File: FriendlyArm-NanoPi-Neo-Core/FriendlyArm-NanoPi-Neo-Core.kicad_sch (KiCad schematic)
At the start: 11 parts, among them J1 Conn_02x12_Odd_Even, J2 Conn_02x12_Odd_Even, J3 Conn_02x10_Odd_Even, J4 USB_OTG, J5 Micro_SD_Card

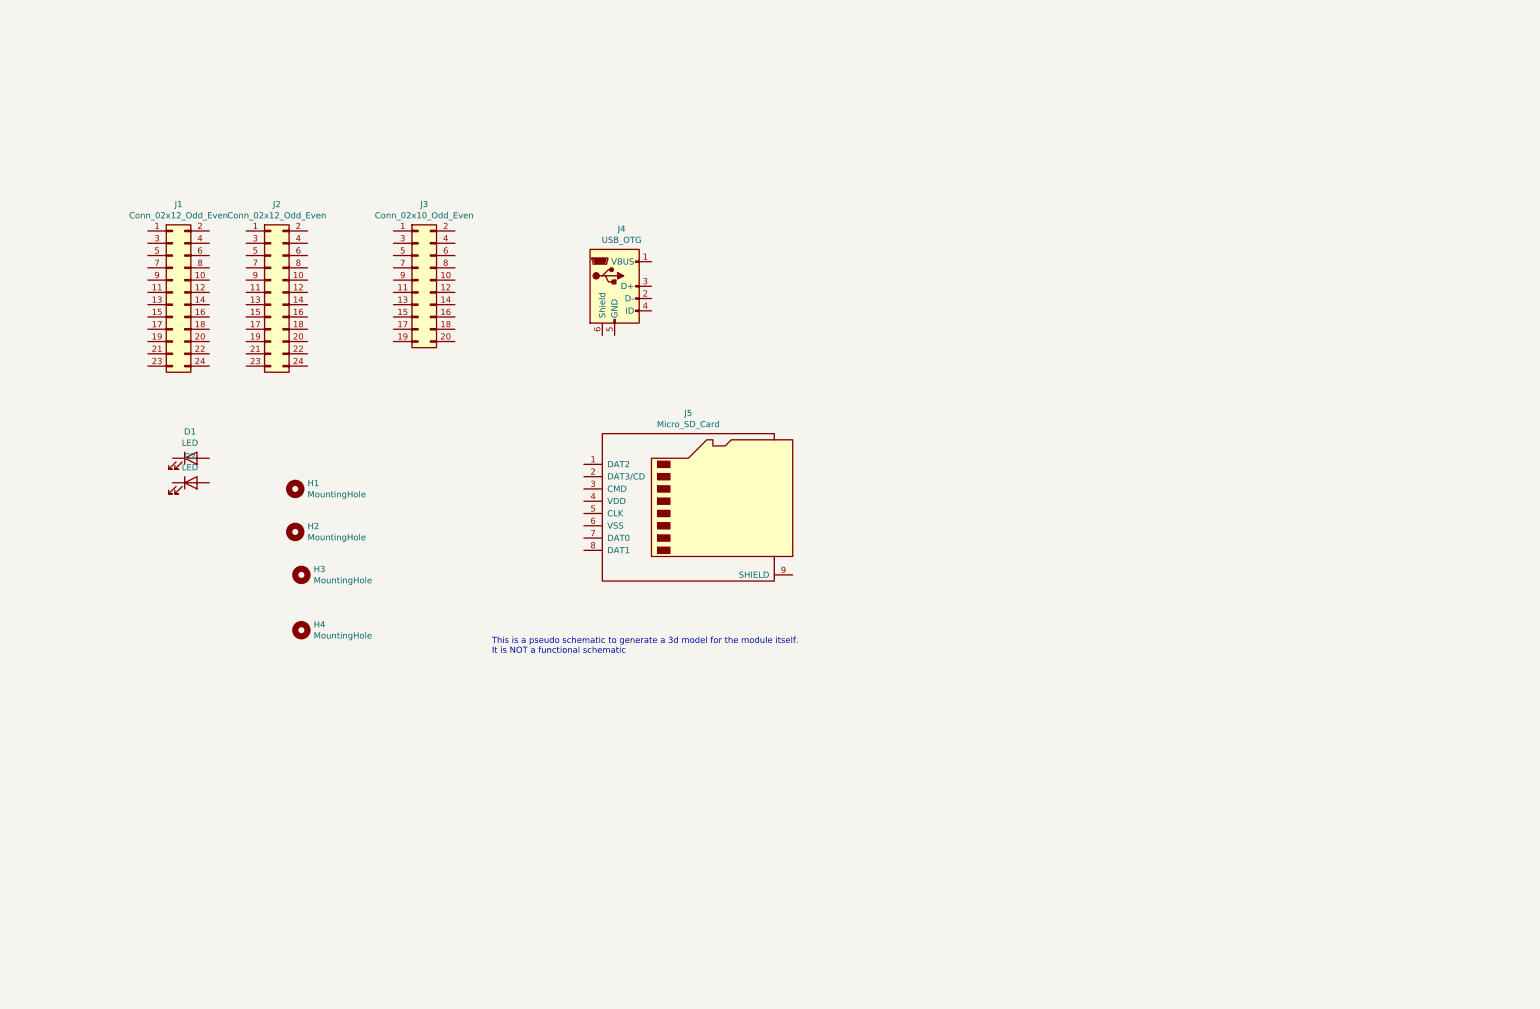
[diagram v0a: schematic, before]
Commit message: nanopi-core: completely overhaul model
Properly numerically align, place all big bgas, label headers
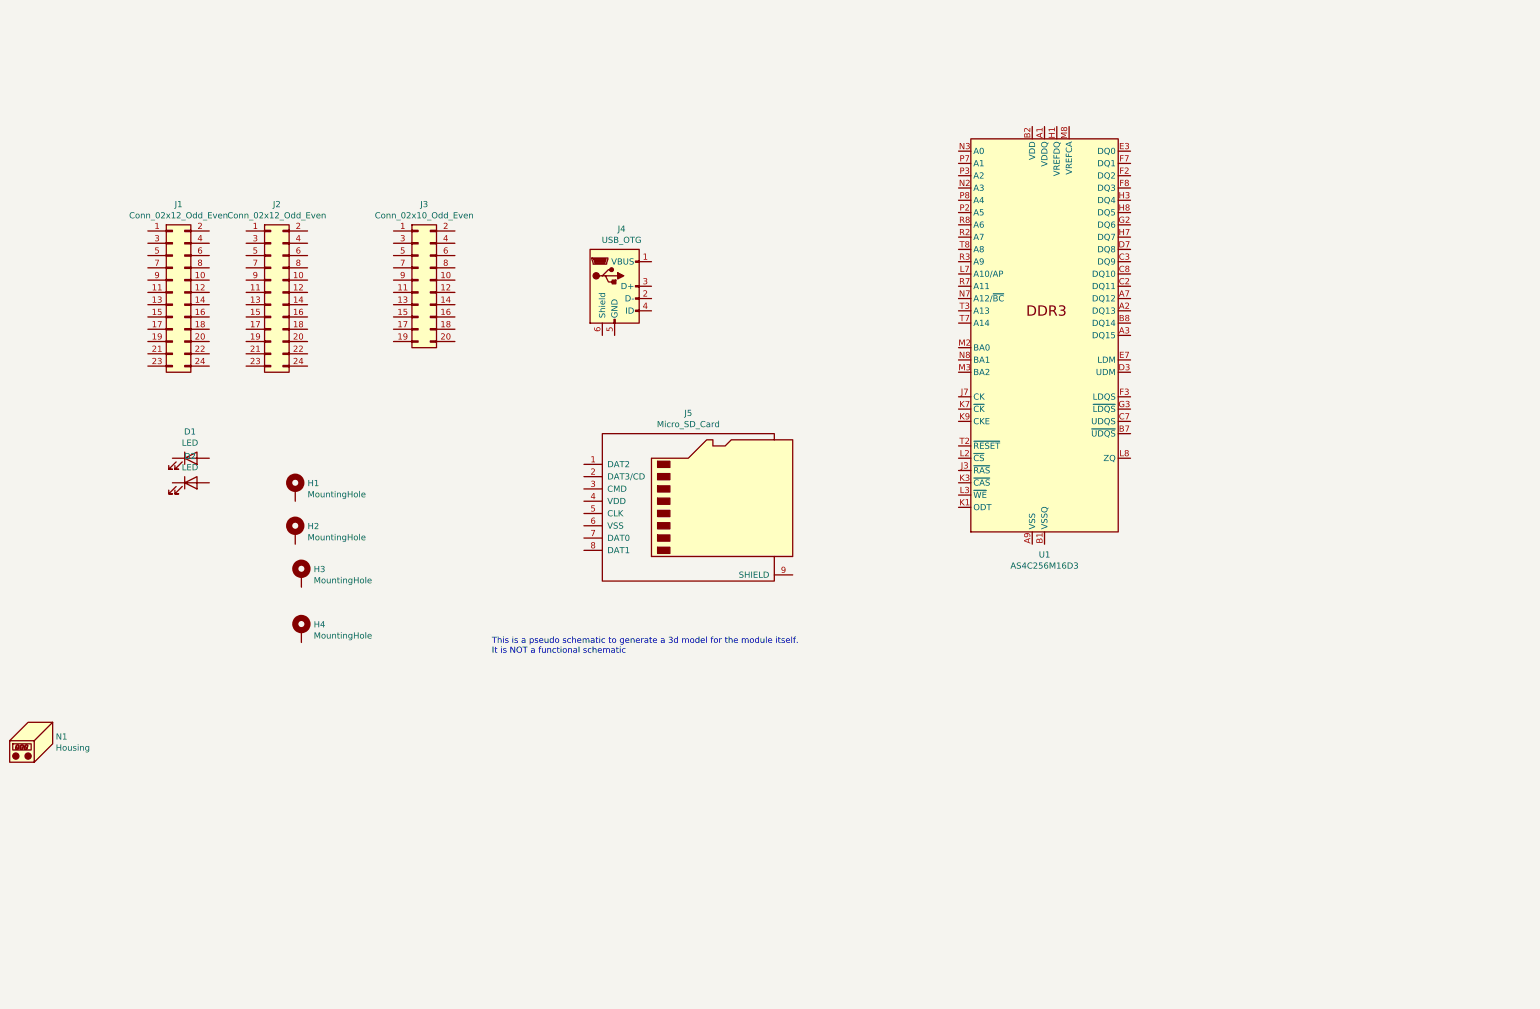
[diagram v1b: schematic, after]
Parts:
- added N1: Housing, Package_BGA:BGA-256_14.0x14.0mm_Layout16x16_P0.8mm_Ball0.45mm_Pad0.32mm_NSMD, symbol Mechanical:Housing
- added U1: AS4C256M16D3, Package_BGA:BGA-96_9.0x13.0mm_Layout2x3x16_P0.8mm, symbol Memory_RAM:AS4C256M16D3
- D1, D2: footprint LED_SMD:LED_0603_1608Metric_Castellated -> LED_SMD:LED_0603_1608Metric
- H1, H2, H3, H4: footprint MountingHole:MountingHole_2.2mm_M2 -> MountingHole:MountingHole_3mm_Pad; symbol Mechanical:MountingHole -> Mechanical:MountingHole_Pad
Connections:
- new net: U1.A1 (VDDQ), U1.A8 (VDDQ), U1.C1 (VDDQ), U1.C9 (VDDQ), U1.D2 (VDDQ), U1.E9 (VDDQ), U1.F1 (VDDQ), U1.H2 (VDDQ), U1.H9 (VDDQ)
- new net: U1.A9 (VSS), U1.B3 (VSS), U1.E1 (VSS), U1.G8 (VSS), U1.J2 (VSS), U1.J8 (VSS), U1.M1 (VSS), U1.M9 (VSS), U1.P1 (VSS), U1.P9 (VSS), U1.T1 (VSS), U1.T9 (VSS)
- new net: U1.B1 (VSSQ), U1.B9 (VSSQ), U1.D1 (VSSQ), U1.D8 (VSSQ), U1.E2 (VSSQ), U1.E8 (VSSQ), U1.F9 (VSSQ), U1.G1 (VSSQ), U1.G9 (VSSQ)
- new net: U1.B2 (VDD), U1.D9 (VDD), U1.G7 (VDD), U1.K2 (VDD), U1.K8 (VDD), U1.N1 (VDD), U1.N9 (VDD), U1.R1 (VDD), U1.R9 (VDD)
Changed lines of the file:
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@@
     (effects (font (size 1.27 1.27)) (justify left bottom))
   )
-  (symbol (lib_id "Mechanical:MountingHole") (at 86.36 97.79 0) (unit 1)
+  (symbol (lib_id "Mechanical:MountingHole_Pad") (at 86.36 97.79 0) (unit 1)
     (in_bom yes) (on_board yes)
     (property "Reference" "H1" (id 0) (at 88.9 96.6216 0)
@@
       (effects (font (size 1.27 1.27)) (justify left))
     )
-    (property "Footprint" "MountingHole:MountingHole_2.2mm_M2" (id 2) (at 86.36 97.79 0)
+    (property "Footprint" "MountingHole:MountingHole_3mm_Pad" (id 2) (at 86.36 97.79 0)
       (effects (font (size 1.27 1.27)) hide)
     )
@@
       (effects (font (size 1.27 1.27)) hide)
     )
-  )
-  (symbol (lib_id "Mechanical:MountingHole") (at 86.36 106.68 0) (unit 1)
+    (pin "1")
+  )
+  (symbol (lib_id "Mechanical:MountingHole_Pad") (at 86.36 106.68 0) (unit 1)
     (in_bom yes) (on_board yes)
     (property "Reference" "H2" (id 0) (at 88.9 105.5116 0)
@@
       (effects (font (size 1.27 1.27)) (justify left))
     )
-    (property "Footprint" "MountingHole:MountingHole_2.2mm_M2" (id 2) (at 86.36 106.68 0)
+    (property "Footprint" "MountingHole:MountingHole_3mm_Pad" (id 2) (at 86.36 106.68 0)
       (effects (font (size 1.27 1.27)) hide)
     )
@@
       (effects (font (size 1.27 1.27)) hide)
     )
-  )
-  (symbol (lib_id "Mechanical:MountingHole") (at 87.63 115.57 0) (unit 1)
+    (pin "1")
+  )
+  (symbol (lib_id "Mechanical:MountingHole_Pad") (at 87.63 115.57 0) (unit 1)
     (in_bom yes) (on_board yes)
     (property "Reference" "H3" (id 0) (at 90.17 114.4016 0)
@@
       (effects (font (size 1.27 1.27)) (justify left))
     )
-    (property "Footprint" "MountingHole:MountingHole_2.2mm_M2" (id 2) (at 87.63 115.57 0)
+    (property "Footprint" "MountingHole:MountingHole_3mm_Pad" (id 2) (at 87.63 115.57 0)
       (effects (font (size 1.27 1.27)) hide)
     )
@@
       (effects (font (size 1.27 1.27)) hide)
     )
-  )
-  (symbol (lib_id "Mechanical:MountingHole") (at 87.63 127 0) (unit 1)
+    (pin "1")
+  )
+  (symbol (lib_id "Mechanical:MountingHole_Pad") (at 87.63 127 0) (unit 1)
     (in_bom yes) (on_board yes)
     (property "Reference" "H4" (id 0) (at 90.17 125.8316 0)
@@
       (effects (font (size 1.27 1.27)) (justify left))
     )
-    (property "Footprint" "MountingHole:MountingHole_2.2mm_M2" (id 2) (at 87.63 127 0)
+    (property "Footprint" "MountingHole:MountingHole_3mm_Pad" (id 2) (at 87.63 127 0)
       (effects (font (size 1.27 1.27)) hide)
     )
@@
       (effects (font (size 1.27 1.27)) hide)
     )
+    (pin "1")
   )
   (symbol (lib_id "Device:LED") (at 64.77 91.44 0) (unit 1)
@@
     (property "Reference" "D1" (id 0) (at 64.5922 85.9536 0))
     (property "Value" "LED" (id 1) (at 64.5922 88.265 0))
-    (property "Footprint" "LED_SMD:LED_0603_1608Metric_Castellated" (id 2) (at 64.77 91.44 0)
+    (property "Footprint" "LED_SMD:LED_0603_1608Metric" (id 2) (at 64.77 91.44 0)
       (effects (font (size 1.27 1.27)) hide)
     )
@@
     (property "Reference" "D2" (id 0) (at 64.5922 91.0336 0))
     (property "Value" "LED" (id 1) (at 64.5922 93.345 0))
-    (property "Footprint" "LED_SMD:LED_0603_1608Metric_Castellated" (id 2) (at 64.77 96.52 0)
+    (property "Footprint" "LED_SMD:LED_0603_1608Metric" (id 2) (at 64.77 96.52 0)
       (effects (font (size 1.27 1.27)) hide)
     )
@@
     (pin "1")
     (pin "2")
+  )
+  (symbol (lib_id "Mechanical:Housing") (at 33.02 149.86 0) (unit 1)
+    (in_bom yes) (on_board yes)
+    (property "Reference" "N1" (id 0) (at 36.8301 149.0281 0)
+      (effects (font (size 1.27 1.27)) (justify left))
+    )
+    (property "Value" "Housing" (id 1) (at 36.8301 151.3268 0)
+      (effects (font (size 1.27 1.27)) (justify left))
+    )
+    (property "Footprint" "Package_BGA:BGA-256_14.0x14.0mm_Layout16x16_P0.8mm_Ball0.45mm_Pad0.32mm_NSMD" (id 2) (at 34.29 148.59 0)
+      (effects (font (size 1.27 1.27)) hide)
+    )
+    (property "Datasheet" "~" (id 3) (at 34.29 148.59 0)
+      (effects (font (size 1.27 1.27)) hide)
+    )
   )
   (symbol (lib_id "Connector:USB_OTG") (at 152.4 55.88 0) (unit 1)
@@
     (pin "9")
   )
+  (symbol (lib_id "Memory_RAM:AS4C256M16D3") (at 241.3 66.04 0) (unit 1)
+    (in_bom yes) (on_board yes)
+    (property "Reference" "U1" (id 0) (at 241.3 111.3854 0))
+    (property "Value" "AS4C256M16D3" (id 1) (at 241.3 113.6841 0))
+    (property "Footprint" "Package_BGA:BGA-96_9.0x13.0mm_Layout2x3x16_P0.8mm" (id 2) (at 240.03 20.32 0)
+      (effects (font (size 1.27 1.27)) hide)
+    )
+    (property "Datasheet" "https://www.alliancememory.com/wp-content/uploads/pdf/ddr3/4GB-AS4C256M16D3.pdf" (id 3) (at 240.03 -2.54 0)
+      (effects (font (size 1.27 1.27)) hide)
+    )
+    (pin "A1")
+    (pin "A8")
+    (pin "A9")
+    (pin "B1")
+    (pin "B2")
+    (pin "B3")
+    (pin "B9")
+    (pin "C1")
+    (pin "C9")
+    (pin "D1")
+    (pin "D2")
+    (pin "D8")
+    (pin "D9")
+    (pin "E1")
+    (pin "E2")
+    (pin "E3")
+    (pin "E8")
+    (pin "E9")
+    (pin "F1")
+    (pin "F2")
+    (pin "F7")
+    (pin "F8")
+    (pin "F9")
+    (pin "G1")
+    (pin "G2")
+    (pin "G7")
+    (pin "G8")
+    (pin "G9")
+    (pin "H1")
+    (pin "H2")
+    (pin "H3")
+    (pin "H7")
+    (pin "H8")
+    (pin "H9")
+    (pin "J2")
+    (pin "J8")
+    (pin "K2")
+    (pin "K8")
+    (pin "L2")
+    (pin "L7")
+    (pin "M1")
+    (pin "M9")
+    (pin "N1")
+    (pin "N2")
+    (pin "N3")
+    (pin "N7")
+    (pin "N9")
+    (pin "P1")
+    (pin "P2")
+    (pin "P3")
+    (pin "P7")
+    (pin "P8")
+    (pin "P9")
+    (pin "R1")
+    (pin "R2")
+    (pin "R3")
+    (pin "R7")
+    (pin "R8")
+    (pin "R9")
+    (pin "T1")
+    (pin "T2")
+    (pin "T3")
+    (pin "T7")
+    (pin "T8")
+    (pin "T9")
+    (pin "A2")
+    (pin "A3")
+    (pin "A7")
+    (pin "B7")
+    (pin "B8")
+    (pin "C2")
+    (pin "C3")
+    (pin "C7")
+    (pin "C8")
+    (pin "D3")
+    (pin "D7")
+    (pin "E7")
+    (pin "F3")
+    (pin "G3")
+    (pin "J1")
+    (pin "J3")
+    (pin "J7")
+    (pin "J9")
+    (pin "K1")
+    (pin "K3")
+    (pin "K7")
+    (pin "K9")
+    (pin "L1")
+    (pin "L3")
+    (pin "L8")
+    (pin "L9")
+    (pin "M2")
+    (pin "M3")
+    (pin "M7")
+    (pin "M8")
+    (pin "N8")
+  )
   (sheet_instances
     (path "/" (page "1"))
@@
   (symbol_instances
     (path "/00000000-0000-0000-0000-00005bf1d529"
-      (reference "D1") (unit 1) (value "LED") (footprint "LED_SMD:LED_0603_1608Metric_Castellated")
+      (reference "D1") (unit 1) (value "LED") (footprint "LED_SMD:LED_0603_1608Metric")
     )
     (path "/00000000-0000-0000-0000-00005bf1d9d2"
-      (reference "D2") (unit 1) (value "LED") (footprint "LED_SMD:LED_0603_1608Metric_Castellated")
+      (reference "D2") (unit 1) (value "LED") (footprint "LED_SMD:LED_0603_1608Metric")
     )
     (path "/00000000-0000-0000-0000-00005befb352"
-      (reference "H1") (unit 1) (value "MountingHole") (footprint "MountingHole:MountingHole_2.2mm_M2")
+      (reference "H1") (unit 1) (value "MountingHole") (footprint "MountingHole:MountingHole_3mm_Pad")
     )
     (path "/00000000-0000-0000-0000-00005befb57d"
-      (reference "H2") (unit 1) (value "MountingHole") (footprint "MountingHole:MountingHole_2.2mm_M2")
+      (reference "H2") (unit 1) (value "MountingHole") (footprint "MountingHole:MountingHole_3mm_Pad")
     )
     (path "/00000000-0000-0000-0000-00005befb66a"
-      (reference "H3") (unit 1) (value "MountingHole") (footprint "MountingHole:MountingHole_2.2mm_M2")
+      (reference "H3") (unit 1) (value "MountingHole") (footprint "MountingHole:MountingHole_3mm_Pad")
     )
     (path "/00000000-0000-0000-0000-00005befb779"
-      (reference "H4") (unit 1) (value "MountingHole") (footprint "MountingHole:MountingHole_2.2mm_M2")
+      (reference "H4") (unit 1) (value "MountingHole") (footprint "MountingHole:MountingHole_3mm_Pad")
     )
     (path "/00000000-0000-0000-0000-00005bef6acb"
@@
       (reference "J5") (unit 1) (value "Micro_SD_Card") (footprint "Connector_Card:microSD_HC_Hirose_DM3D-SF")
     )
-  )
+    (path "/e8a2b6ce-d3f0-4eb3-a9a7-47629f12dac4"
+      (reference "N1") (unit 1) (value "Housing") (footprint "Package_BGA:BGA-256_14.0x14.0mm_Layout16x16_P0.8mm_Ball0.45mm_Pad0.32mm_NSMD")
+    )
+    (path "/22fe7d2a-5cd5-405a-9a0a-20a473bd5676"
+      (reference "U1") (unit 1) (value "AS4C256M16D3") (footprint "Package_BGA:BGA-96_9.0x13.0mm_Layout2x3x16_P0.8mm")
+    )
+  )

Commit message: nano-pi neo core: fix emmc, add parts on edge
There's a fairly high sot23 part rigth on the edge that you may want to
be careful with if you're cramming things....

Also, this uses a proper model for the emmc that is positioned better
and has the right heights.
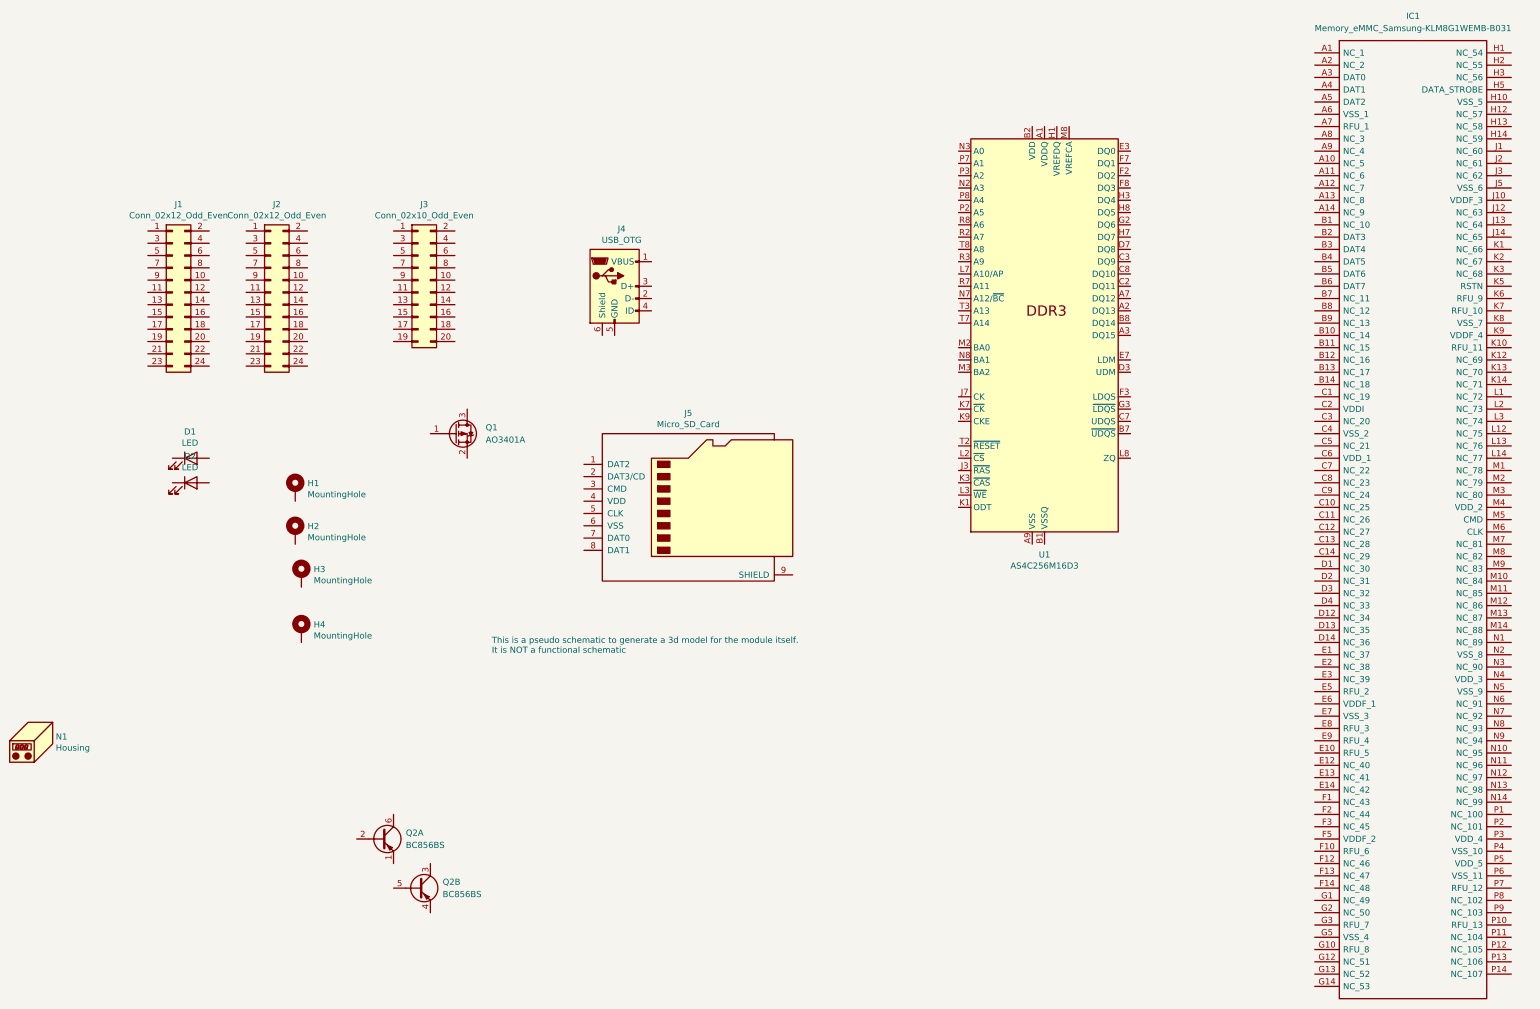
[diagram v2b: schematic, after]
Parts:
- added IC1: Memory_eMMC_Samsung-KLM8G1WEMB-B031, et-parts:BGA153_P0.5mm_14X14_11.5x13.0mm_h0.8mm_Samsung_eMMC, symbol etactica-parts:Memory_eMMC_Samsung-KLM8G1WEMB-B031
- added Q1: AO3401A, Package_TO_SOT_SMD:SOT-23, symbol Transistor_FET:AO3401A
- added Q2: BC856BS, Package_TO_SOT_SMD:SOT-363_SC-70-6, symbol Transistor_BJT:BC856BS
